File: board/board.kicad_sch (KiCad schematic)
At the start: 3 parts, among them J1 022_battery_cells, J2 022_battery_cells

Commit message: added custom footprint
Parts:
- J1: footprint (none) -> on_edge:on_edge_2x05_device
- J2: footprint (none) -> on_edge:on_edge_2x05_host
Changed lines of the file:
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@@
     (property "Reference" "J1" (id 0) (at 131.445 111.76 0))
     (property "Value" "022_battery_cells" (id 1) (at 131.445 114.3 0))
-    (property "Footprint" "" (id 2) (at 123.19 113.03 0)
+    (property "Footprint" "on_edge:on_edge_2x05_device" (id 2) (at 123.19 113.03 0)
       (effects (font (size 1.27 1.27)) hide)
     )
@@
       (effects (font (size 1.27 1.27)) (justify left))
     )
-    (property "Footprint" "" (id 2) (at 213.995 111.76 0)
+    (property "Footprint" "on_edge:on_edge_2x05_host" (id 2) (at 213.995 111.76 0)
       (effects (font (size 1.27 1.27)) hide)
     )
@@
     )
     (path "/75bd16b2-0277-4536-a692-5a43581ae4c0"
-      (reference "J1") (unit 1) (value "022_battery_cells") (footprint "")
+      (reference "J1") (unit 1) (value "022_battery_cells") (footprint "on_edge:on_edge_2x05_device")
     )
     (path "/83850f46-fbc7-4737-a426-703cfefbdd02"
-      (reference "J2") (unit 1) (value "022_battery_cells") (footprint "")
+      (reference "J2") (unit 1) (value "022_battery_cells") (footprint "on_edge:on_edge_2x05_host")
     )
     (path "/b72b6f4a-7489-40f2-bb90-d75ae01aa368"

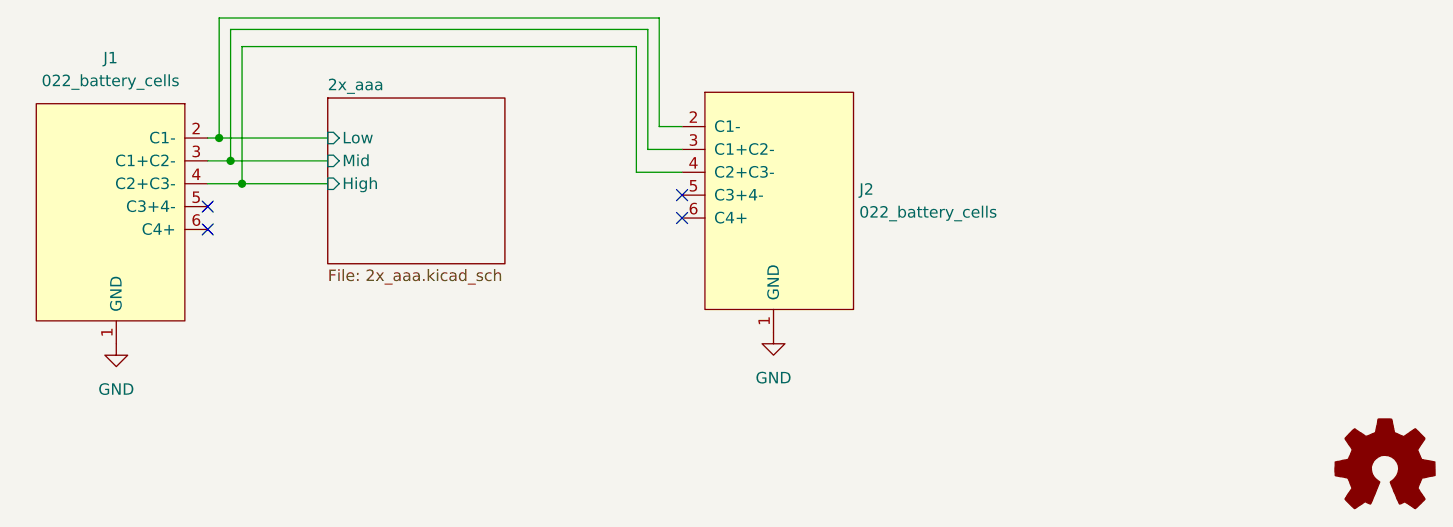
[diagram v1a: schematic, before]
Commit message: added silkscreen + and - so that the pattery polarization is clear. added resistor for connection to GND if needed
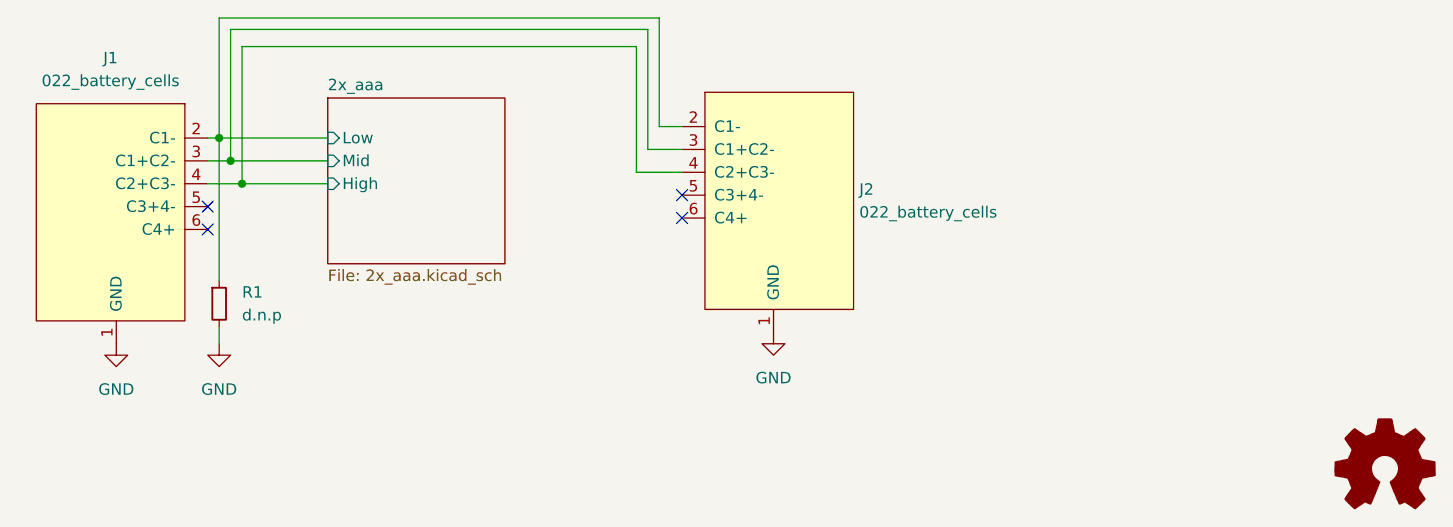
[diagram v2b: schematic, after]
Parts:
- added R1: d.n.p, Resistor_SMD:R_0805_2012Metric, symbol Device:R_Small
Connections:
- net 2x_aaa/Low: now also R1.1
- net GND: now also R1.2
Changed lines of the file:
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@@
+    (stroke (width 0) (type default) (color 0 0 0 0))
+  )
+  (wire (pts (xy 143.51 141.605) (xy 143.51 143.51))
     (stroke (width 0) (type default) (color 0 0 0 0))
   )
@@
   )
   (wire (pts (xy 146.05 125.73) (xy 146.05 110.49))
+    (stroke (width 0) (type default) (color 0 0 0 0))
+  )
+  (wire (pts (xy 143.51 120.65) (xy 143.51 136.525))
     (stroke (width 0) (type default) (color 0 0 0 0))
   )
@@
   (wire (pts (xy 144.78 108.585) (xy 144.78 123.19))
     (stroke (width 0) (type default) (color 0 0 0 0))
+  )
+  (symbol (lib_id "Device:R_Small") (at 143.51 139.065 0) (unit 1)
+    (in_bom yes) (on_board yes) (fields_autoplaced)
+    (property "Reference" "R1" (id 0) (at 146.05 137.7949 0)
+      (effects (font (size 1.27 1.27)) (justify left))
+    )
+    (property "Value" "d.n.p" (id 1) (at 146.05 140.3349 0)
+      (effects (font (size 1.27 1.27)) (justify left))
+    )
+    (property "Footprint" "Resistor_SMD:R_0805_2012Metric" (id 2) (at 143.51 139.065 0)
+      (effects (font (size 1.27 1.27)) hide)
+    )
+    (property "Datasheet" "~" (id 3) (at 143.51 139.065 0)
+      (effects (font (size 1.27 1.27)) hide)
+    )
+    (pin "1")
+    (pin "2")
+  )
+  (symbol (lib_id "power:GND") (at 143.51 143.51 0) (unit 1)
+    (in_bom yes) (on_board yes) (fields_autoplaced)
+    (property "Reference" "#PWR0103" (id 0) (at 143.51 149.86 0)
+      (effects (font (size 1.27 1.27)) hide)
+    )
+    (property "Value" "GND" (id 1) (at 143.51 148.59 0))
+    (property "Footprint" "" (id 2) (at 143.51 143.51 0)
+      (effects (font (size 1.27 1.27)) hide)
+    )
+    (property "Datasheet" "" (id 3) (at 143.51 143.51 0)
+      (effects (font (size 1.27 1.27)) hide)
+    )
+    (pin "1")
   )
   (symbol (lib_id "power:GND") (at 205.105 142.24 0) (unit 1)
@@
       (reference "#PWR0102") (unit 1) (value "GND") (footprint "")
     )
+    (path "/163fda79-70fc-4177-be70-f2f1412f88bd"
+      (reference "#PWR0103") (unit 1) (value "GND") (footprint "")
+    )
     (path "/75bd16b2-0277-4536-a692-5a43581ae4c0"
       (reference "J1") (unit 1) (value "022_battery_cells") (footprint "on_edge:on_edge_2x05_device")
@@
       (reference "LOGO1") (unit 1) (value "Logo_Open_Hardware_Small") (footprint "Symbol:OSHW-Symbol_6.7x6mm_SilkScreen")
     )
+    (path "/106668f8-89ac-48d7-b9c1-e039418c23a8"
+      (reference "R1") (unit 1) (value "d.n.p") (footprint "Resistor_SMD:R_0805_2012Metric")
+    )
     (path "/767ce4c6-0e55-4543-92f0-34cb8237a544/178eb12c-d345-4973-b09a-232f8f5bbcf8"
